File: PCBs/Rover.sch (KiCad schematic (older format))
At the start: 32 parts

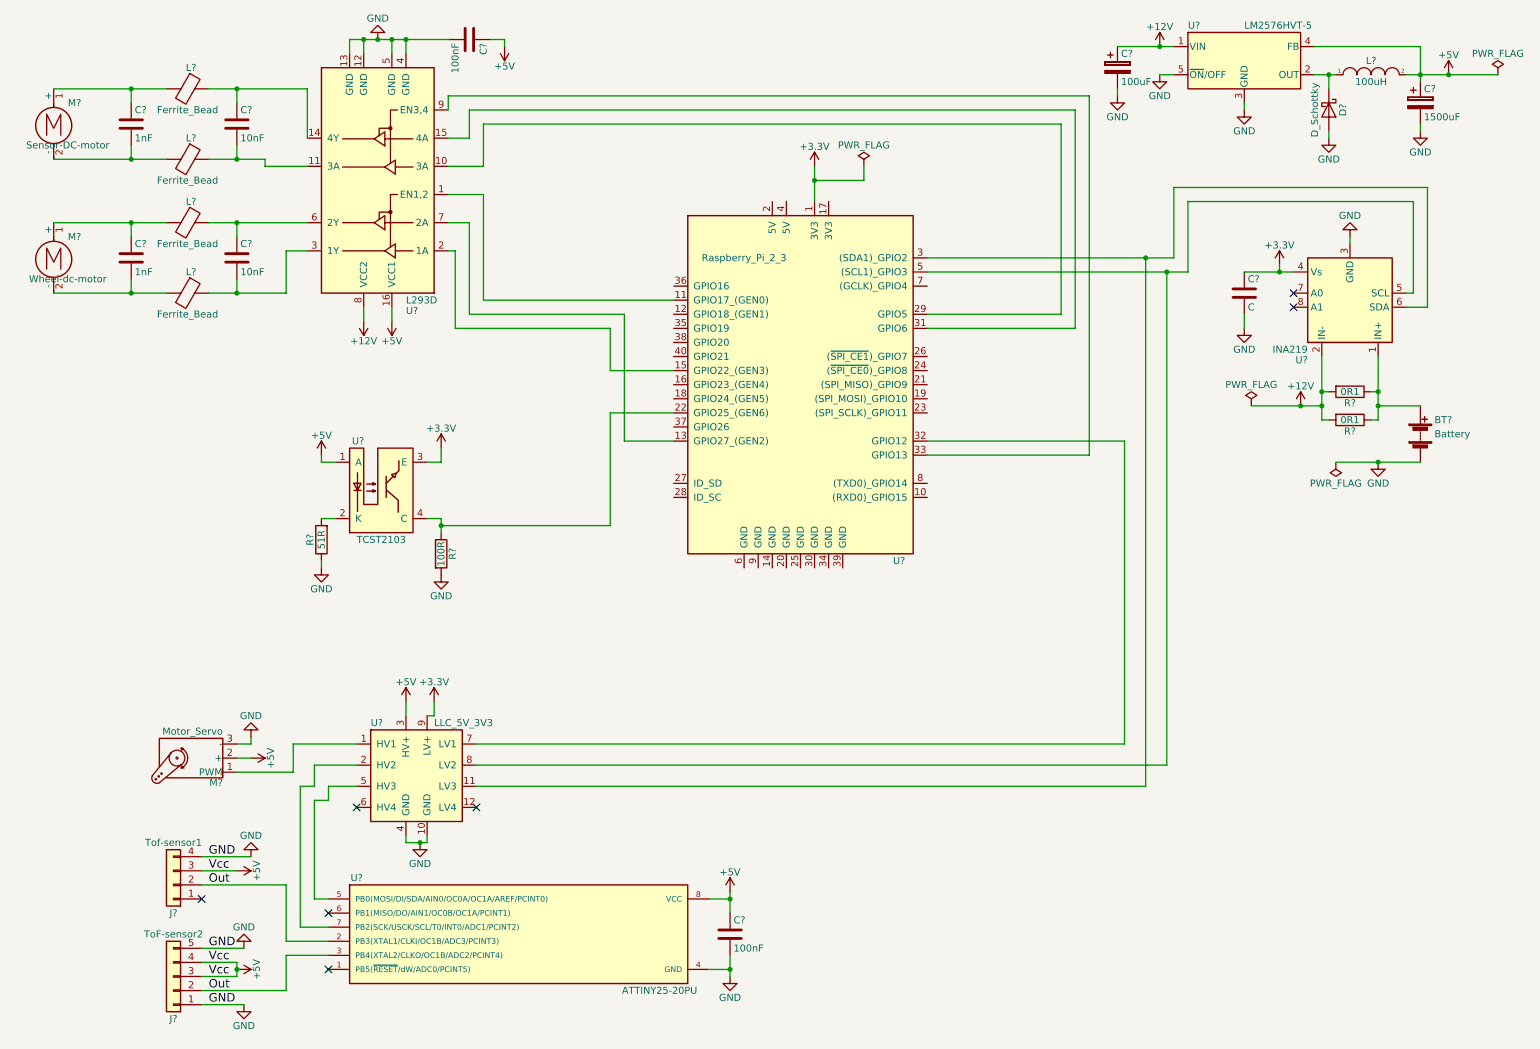
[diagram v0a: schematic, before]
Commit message: percentage added to the application and motor and servo drivers tested on RPi
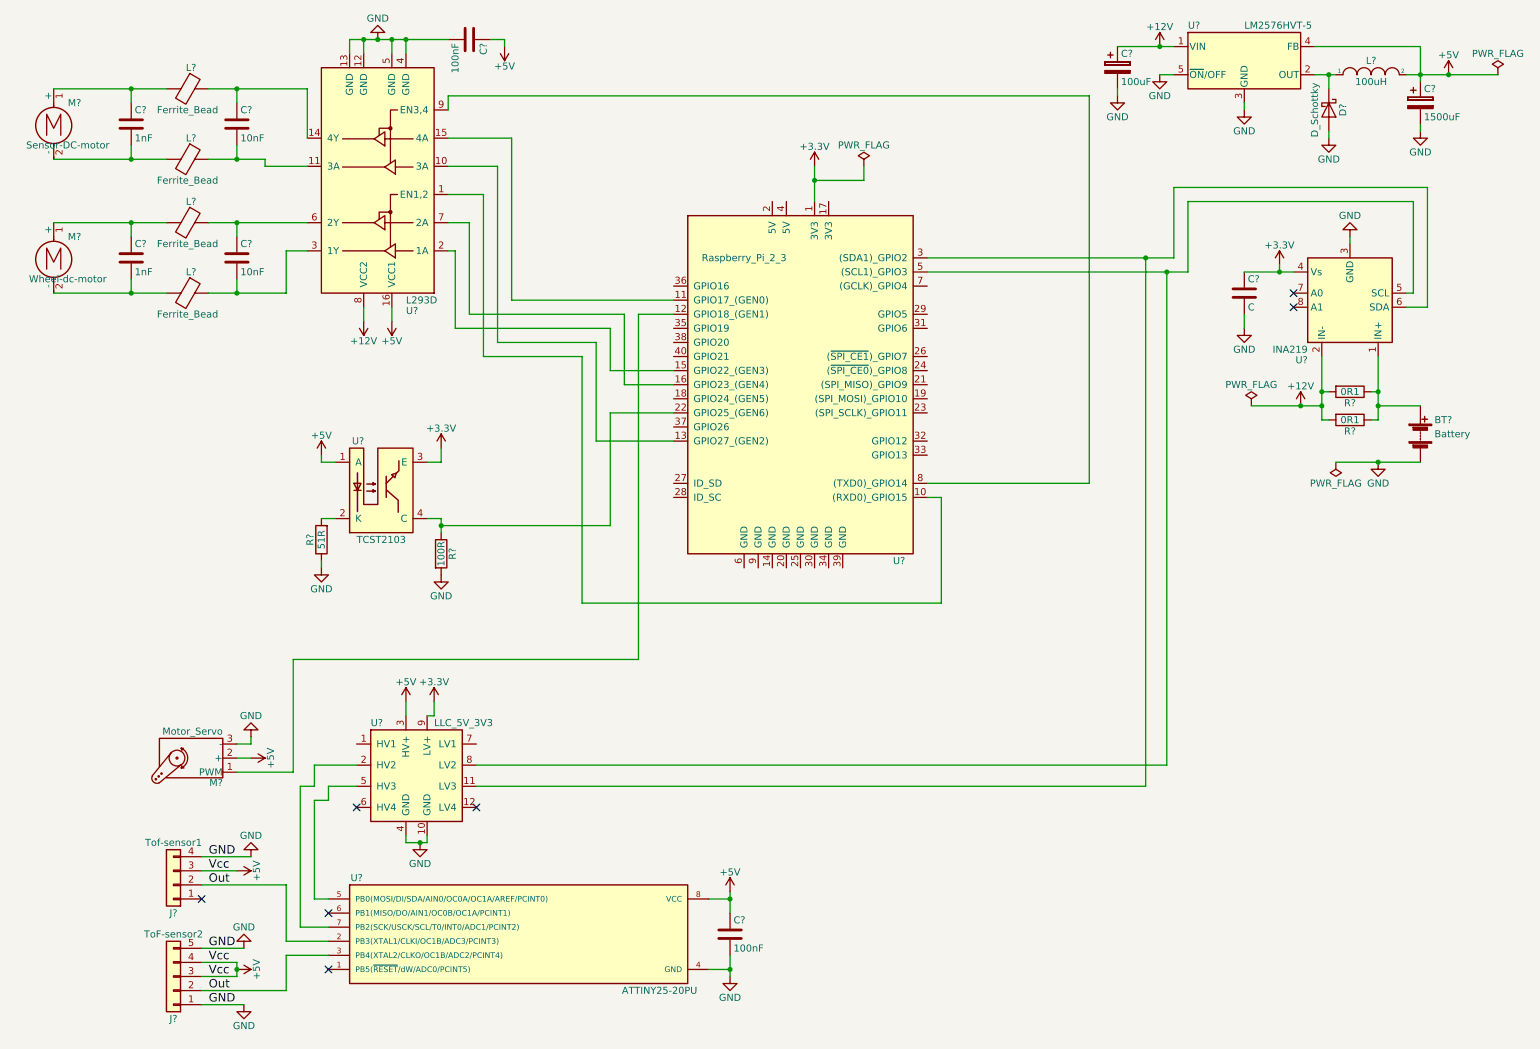
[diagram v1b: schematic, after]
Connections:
- net at U?.10 ((RXD0)_GPIO15): now also U?.1 (EN1,2)
- net at U?.11 (GPIO17_(GEN0)): now also U?.15 (4A); no longer U?.1 (EN1,2)
- net at U?.12 (GPIO18_(GEN1)): now also M?.1 (PWM)
- net at U?.13 (GPIO27_(GEN2)): now also U?.10 (3A); no longer U?.7 (2A)
- net at U?.16 (GPIO23_(GEN4)): now also U?.7 (2A)
- net at U?.29 (GPIO5): no longer U?.10 (3A)
- net at U?.31 (GPIO6): no longer U?.15 (4A)
- net at U?.32 (GPIO12): no longer U?.7 (LV1)
- net at U?.33 (GPIO13): no longer U?.9 (EN3,4)
- net at U?.8 ((TXD0)_GPIO14): now also U?.9 (EN3,4)
- net at U?.1 (HV1): no longer M?.1 (PWM)
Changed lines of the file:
@@
 	9200 2750 9200 2650
 Wire Wire Line
-	2900 5700 2450 5700
-Wire Wire Line
-	2450 5700 2450 5900
+	2450 5100 2450 5900
 Wire Wire Line
 	2450 5900 2050 5900
@@
 	8700 2250 8700 1750
 Wire Wire Line
-	8800 1850 8800 2350
+	8800 2350 8800 1850
 Wire Wire Line
-	8800 2350 6950 2350
+	6950 2350 8800 2350
 Wire Wire Line
 	8650 2350 8650 5850
@@
 Connection ~ 8500 2250
 Wire Wire Line
-	3500 4200 3500 4100
-Wire Wire Line
-	6950 3550 8350 3550
-Wire Wire Line
-	8350 3550 8350 5700
-Wire Wire Line
-	8350 5700 3750 5700
+	3500 4100 3500 4200
 Connection ~ 3250 700
 Wire Wire Line
 	3950 700  3950 750
 Wire Wire Line
-	8100 1100 8100 3650
+	8100 1100 8100 3850
 Wire Wire Line
-	8100 3650 6950 3650
+	3550 1600 3900 1600
 Wire Wire Line
-	6950 2650 7900 2650
-Wire Wire Line
-	7900 2650 7900 1300
-Wire Wire Line
-	7900 1300 3800 1300
-Wire Wire Line
-	3800 1300 3800 1600
-Wire Wire Line
-	3800 1600 3550 1600
-Wire Wire Line
-	6950 2750 8000 2750
-Wire Wire Line
-	8000 2750 8000 1200
-Wire Wire Line
-	8000 1200 3700 1200
-Wire Wire Line
-	3700 1200 3700 1400
-Wire Wire Line
-	3700 1400 3550 1400
+	3550 1400 4000 1400
 Wire Wire Line
 	8100 1100 3550 1100
@@
 	3550 1100 3550 1200
 Wire Wire Line
-	5150 2550 3800 2550
-Wire Wire Line
-	3800 2550 3800 1800
+	3800 1800 3800 2950
 Wire Wire Line
 	3800 1800 3550 1800
-Wire Wire Line
-	5150 3550 4800 3550
-Wire Wire Line
-	4800 3550 4800 2650
 Wire Wire Line
 	4800 2650 3700 2650
@@
 	4700 4150 3500 4150
 Connection ~ 3500 4150
+Wire Wire Line
+	4800 2650 4800 3150
+Wire Wire Line
+	4800 3150 5150 3150
+Wire Wire Line
+	4000 1400 4000 2550
+Wire Wire Line
+	4000 2550 5150 2550
+Wire Wire Line
+	3900 1600 3900 2850
+Wire Wire Line
+	3900 2850 4600 2850
+Wire Wire Line
+	4600 2850 4600 3550
+Wire Wire Line
+	4600 3550 5150 3550
+Wire Wire Line
+	2450 5100 4900 5100
+Wire Wire Line
+	4900 5100 4900 2650
+Wire Wire Line
+	4900 2650 5150 2650
+Wire Wire Line
+	6950 3950 7050 3950
+Wire Wire Line
+	7050 3950 7050 4700
+Wire Wire Line
+	7050 4700 4500 4700
+Wire Wire Line
+	4500 4700 4500 2950
+Wire Wire Line
+	4500 2950 3800 2950
+Wire Wire Line
+	8100 3850 6950 3850
 $EndSCHEMATC

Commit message: edited schematics, progress on the Rover software
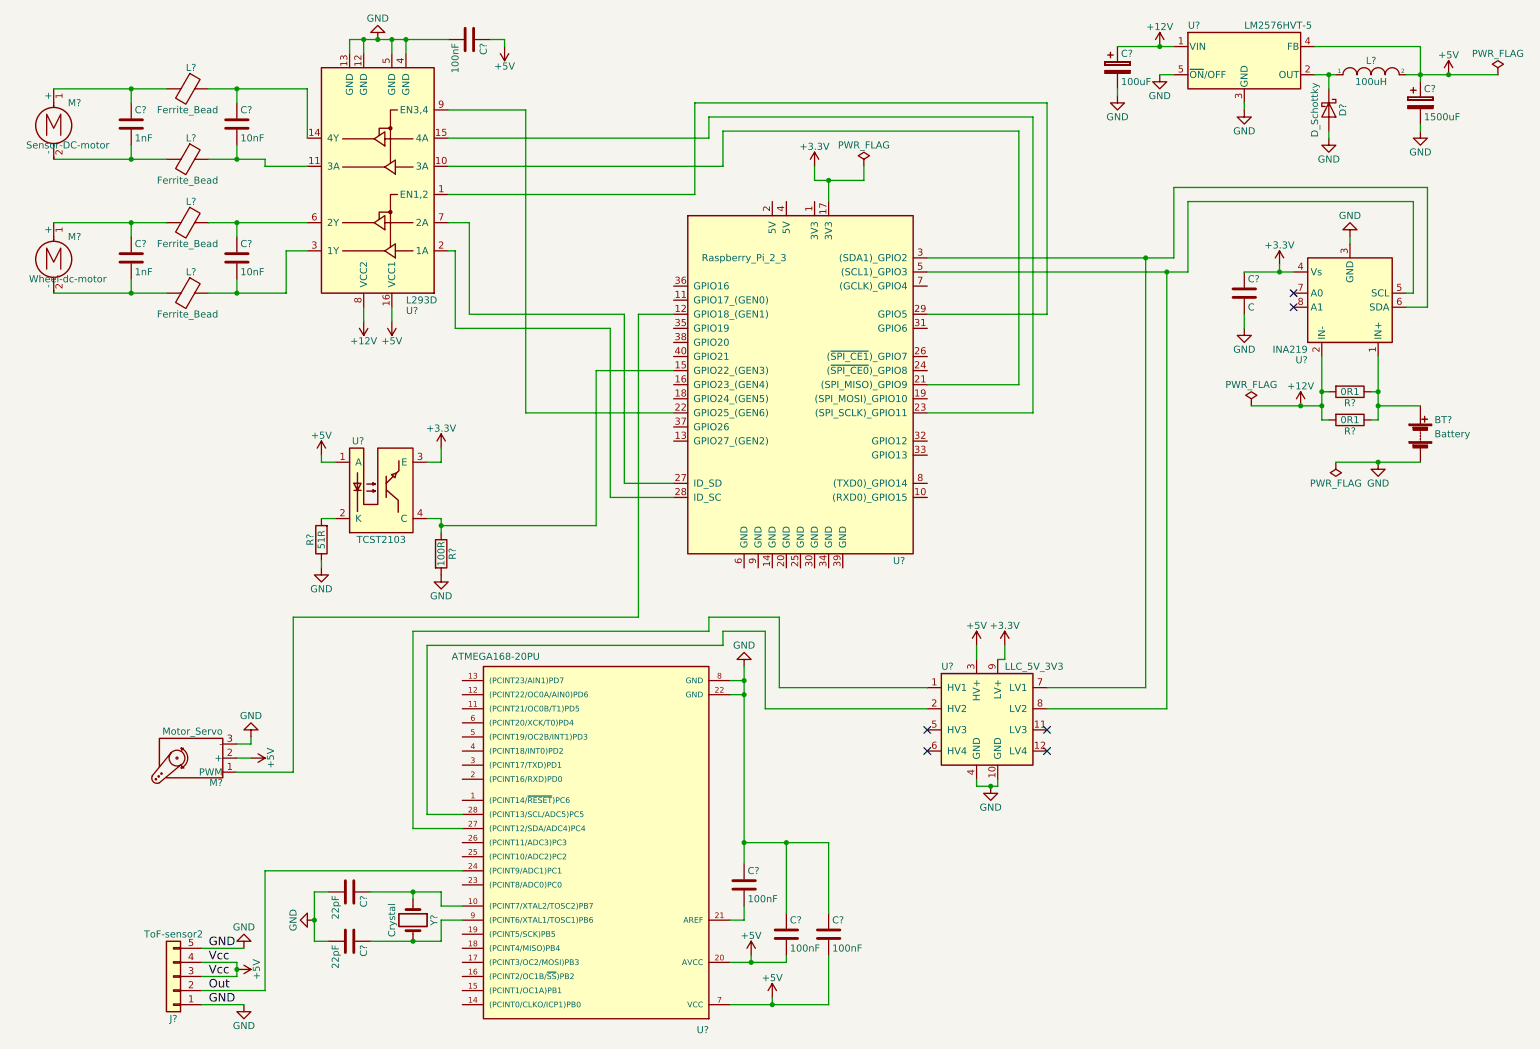
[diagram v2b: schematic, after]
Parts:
- removed C?: 100nF, symbol C
- removed J?: Tof-sensor1, symbol Conn_01x04
- removed U?: ATTINY25-20PU, Housings_DIP:DIP-8_W7.62mm, symbol ATTINY25-20PU
- added C? (x2): 22pF, symbol C
- added C? (x3): 100nF, symbol C
- added U?: ATMEGA168-20PU, DIL28, symbol ATMEGA168-20PU
- added Y?: Crystal, symbol Crystal
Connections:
- net +3V3: now also U?.17 (3V3); no longer U?.1 (3V3)
- net +5V: now also C?.2, C?.2, U?.20 (AVCC), U?.7 (VCC)
- net GND: now also C?.1, C?.1, C?.1, C?.2, C?.2, U?.22 (GND), U?.8 (GND)
- net Out: now also U?.24 ((PCINT9/ADC1)PC1)
- net at U?.10 ((RXD0)_GPIO15): no longer U?.1 (EN1,2)
- net at U?.11 (GPIO17_(GEN0)): no longer U?.15 (4A)
- net at U?.13 (GPIO27_(GEN2)): no longer U?.10 (3A)
- net at U?.15 (GPIO22_(GEN3)): now also R?.1, U?.4 (C); no longer U?.2 (1A)
- net at U?.16 (GPIO23_(GEN4)): no longer U?.7 (2A)
- net at U?.21 ((SPI_MISO)_GPIO9): now also U?.10 (3A)
- net at U?.23 ((SPI_SCLK)_GPIO11): now also U?.15 (4A)
- net at U?.27 (ID_SD): now also U?.7 (2A)
- net at U?.28 (ID_SC): now also U?.2 (1A)
- net at U?.29 (GPIO5): now also U?.1 (EN1,2)
- net at U?.3 ((SDA1)_GPIO2), U?.6 (SDA): now also U?.7 (LV1); no longer U?.11 (LV3)
- net at U?.9 (EN3,4): now also U?.22 (GPIO25_(GEN6)); no longer U?.8 ((TXD0)_GPIO14)
- net at U?.2 (HV2): now also U?.28 ((PCINT13/SCL/ADC5)PC5)
- net at U?.1 (HV1): now also U?.27 ((PCINT12/SDA/ADC4)PC4)
- new net: C?.1, U?.10 ((PCINT7/XTAL2/TOSC2)PB7), Y?.1
- new net: C?.2, U?.21 (AREF)
- new net: C?.1, U?.9 ((PCINT6/XTAL1/TOSC1)PB6), Y?.2
- no-connect marks 7 -> 6
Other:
- moved on the sheet: U?

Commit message: md edit
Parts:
- R?: value 51R -> 75R
- R?: value 100R -> 1k
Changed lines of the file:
@@
 P 2650 4250
 F 0 "R?" V 2730 4250 50  0000 C CNN
-F 1 "51R" V 2650 4250 50  0000 C CNN
+F 1 "75R" V 2650 4250 50  0000 C CNN
 F 2 "" V 2580 4250 50  0001 C CNN
 F 3 "" H 2650 4250 50  0001 C CNN
@@
 P 3500 4350
 F 0 "R?" V 3580 4350 50  0000 C CNN
-F 1 "100R" V 3500 4350 50  0000 C CNN
+F 1 "1k" V 3500 4350 50  0000 C CNN
 F 2 "" V 3430 4350 50  0001 C CNN
 F 3 "" H 3500 4350 50  0001 C CNN
